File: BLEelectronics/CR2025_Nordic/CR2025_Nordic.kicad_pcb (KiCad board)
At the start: 2 copper layers, 24 parts, among them Q1 Si2307CDS, U1 LP5907MFX-3.3, U2 BAT-HLD-001, U3 LTC4412xS6, U4 LTC4054LES5-4.2#TRPBF, U5 MX25R6435FM2IL0

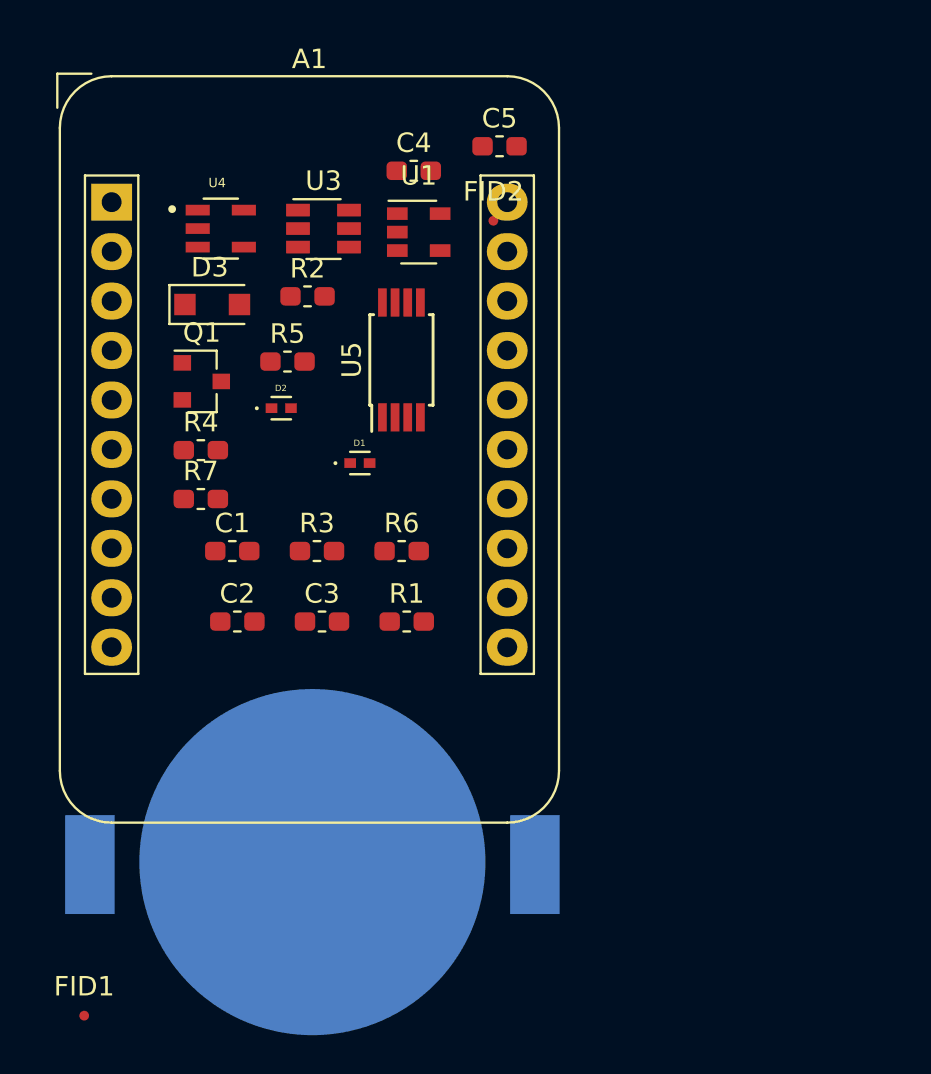
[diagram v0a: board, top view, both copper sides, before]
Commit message: Completed Nordic Dongle adaptor. DRC clean. Ready for review
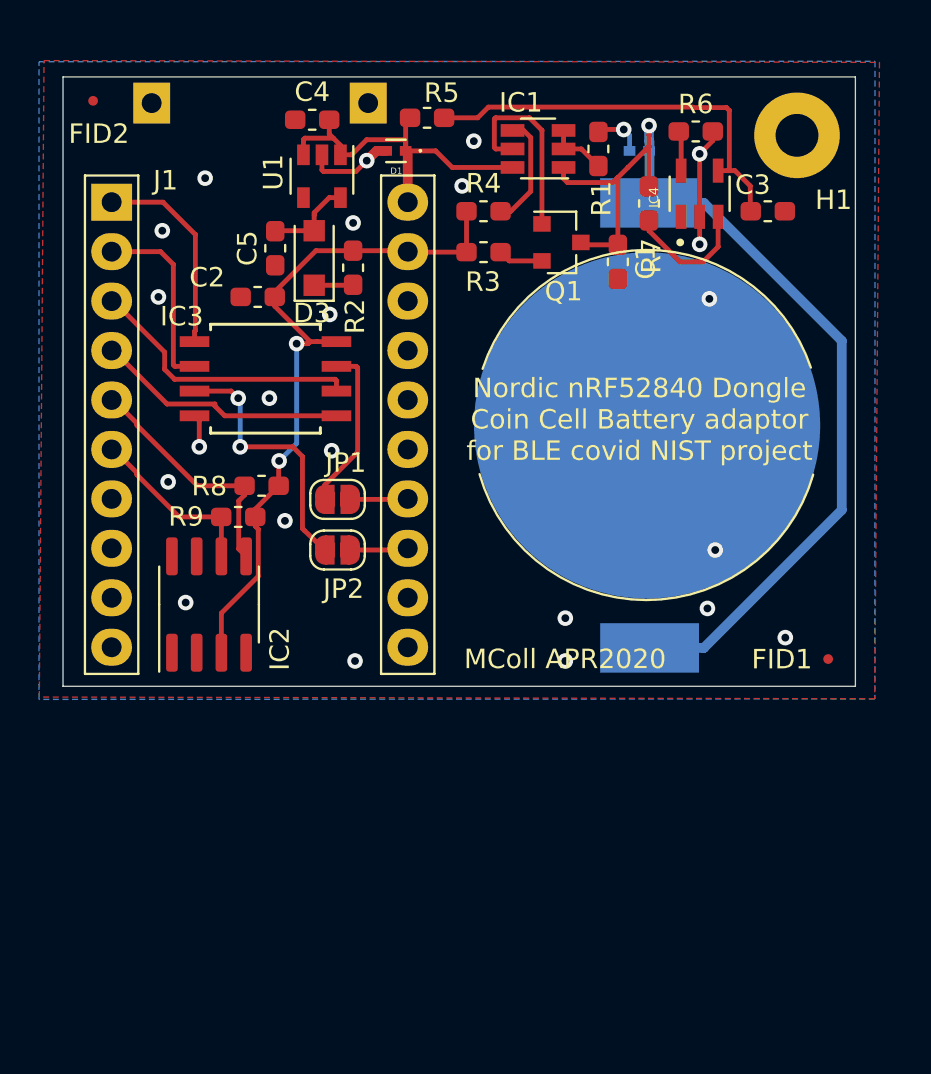
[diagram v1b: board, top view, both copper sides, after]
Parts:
- removed U5: MX25R6435FM2IL0, Package_SO:TSSOP-8_4.4x3mm_P0.65mm
- added H1: MountingHole, MountingHole:MountingHole_2.2mm_M2_Pad, F.Cu at (162.0, 75.7)
- added IC2: PCF8523T, Package_SO:SOIC-8_3.9x4.9mm_P1.27mm, F.Cu at (131.8, 99.8)
- added IC3: MX25R6435FM2IL0, 0my_footprints:MX25R6435FM2IL0, F.Cu at (134.7, 88.2)
- added JP1: Jumper_2_Open, Jumper:SolderJumper-2_P1.3mm_Open_RoundedPad1.0x1.5mm, F.Cu at (138.4, 94.4)
- added JP2: Jumper_2_Open, Jumper:SolderJumper-2_P1.3mm_Open_RoundedPad1.0x1.5mm, F.Cu at (138.4, 97.0)
- added R8: 4.7K, Resistor_SMD:R_0603_1608Metric_Pad1.05x0.95mm_HandSolder, F.Cu at (134.5, 93.7)
- added R9: 4.7K, Resistor_SMD:R_0603_1608Metric_Pad1.05x0.95mm_HandSolder, F.Cu at (133.3, 95.3)
- D2: moved to B.Cu
- J1: renamed from A1; footprint Module:Adafruit_HUZZAH_ESP8266_breakout -> 0my_footprints:Nordic_nRF52840_FeatherHeader
- moved FID1 42.4 mm to (163.6, 102.6)
- moved C3 31.1 mm to (160.5, 79.6)
- moved U2 28.3 mm to (154.3, 90.6), turned to 90 degrees
- moved R7 27.6 mm to (154.4, 79.2), turned to 270 degrees
- moved R6 26.3 mm to (156.8, 75.5)
- moved R1 26.2 mm to (151.8, 76.4), turned to 90 degrees
- moved C1 24.8 mm to (152.8, 82.2), turned to 270 degrees
- moved IC4 24.7 mm to (157.0, 78.7), turned to 90 degrees
- moved D2 22.6 mm to (153.9, 76.5)
- moved FID2 21.5 mm to (125.8, 73.9)
- moved Q1 19.8 mm to (149.9, 81.2)
- moved R4 19.0 mm to (145.9, 79.6)
- moved R3 17.6 mm to (145.9, 81.7)
- moved C2 16.7 mm to (134.3, 84.0), turned to 180 degrees
- moved D1 16.1 mm to (141.4, 76.5), turned to 180 degrees
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- renumbered U3 to IC1, U4 to IC4
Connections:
- C4 pad 2: Net-(C4-Pad2) -> /5Vusb
- D3 pad 1: Net-(C4-Pad2) -> Net-(D3-Pad1)
- D3 pad 2: /5Vusb -> Net-(C5-Pad2)
- J1 pad 1: Net-(A1-Pad1) -> /CS
- J1 pad 2: Net-(A1-Pad2) -> /SO
- J1 pad 3: Net-(A1-Pad3) -> /SCLK
- J1 pad 4: Net-(A1-Pad4) -> /SI
- J1 pad 5: Net-(A1-Pad5) -> /SDA
- J1 pad 6: Net-(A1-Pad6) -> /SCL
- R2 pad 2: Net-(C5-Pad2) -> Net-(D3-Pad1)
- U1 pad 1: Net-(C4-Pad2) -> /5Vusb
- U1 pad 2: Net-(U1-Pad2) -> GND
- U1 pad 3: Net-(C4-Pad2) -> /5Vusb
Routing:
- net /3V: track 0.00 -> 53.0 mm, vias 0 -> 1
- net /VDD_3V: track 0.00 -> 35.9 mm, vias 0 -> 2
- net Net-(C3-Pad1): track 0.00 -> 21.3 mm
- net /5Vusb: track 0.00 -> 18.9 mm
- net GND: track 0.00 -> 15.2 mm, vias 0 -> 24
- net /SCLK: track 0.00 -> 14.3 mm
- net /WP: track 0.00 -> 13.9 mm, vias 0 -> 2
- net /SI: track 0.00 -> 13.0 mm
- net /SDA: track 0.00 -> 12.6 mm
- net /CS: track 0.00 -> 10.5 mm
- net Net-(IC1-Pad5): track 0.00 -> 9.97 mm
- net /SO: track 0.00 -> 9.72 mm
- net /SCL: track 0.00 -> 9.15 mm
- net /RESET: track 0.00 -> 8.57 mm
- net Net-(IC4-Pad3): track 0.00 -> 6.60 mm
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- added copper zone on B.Cu, net GND
- added copper zone on F.Cu, net GND
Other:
- board outline added: 40.7 x 31.3 mm
- board text added: "MColl APR2020"
- board text added: "Nordic nRF52840 Dongle Coin Cell Battery adaptor for BLE covid NIST project"

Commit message: Updated schematic: jumper bypass MOSFET, clock out to header, WP moved to fast IO, fixed library refs, ass spare MOSFET from LTC4412 datasheet.
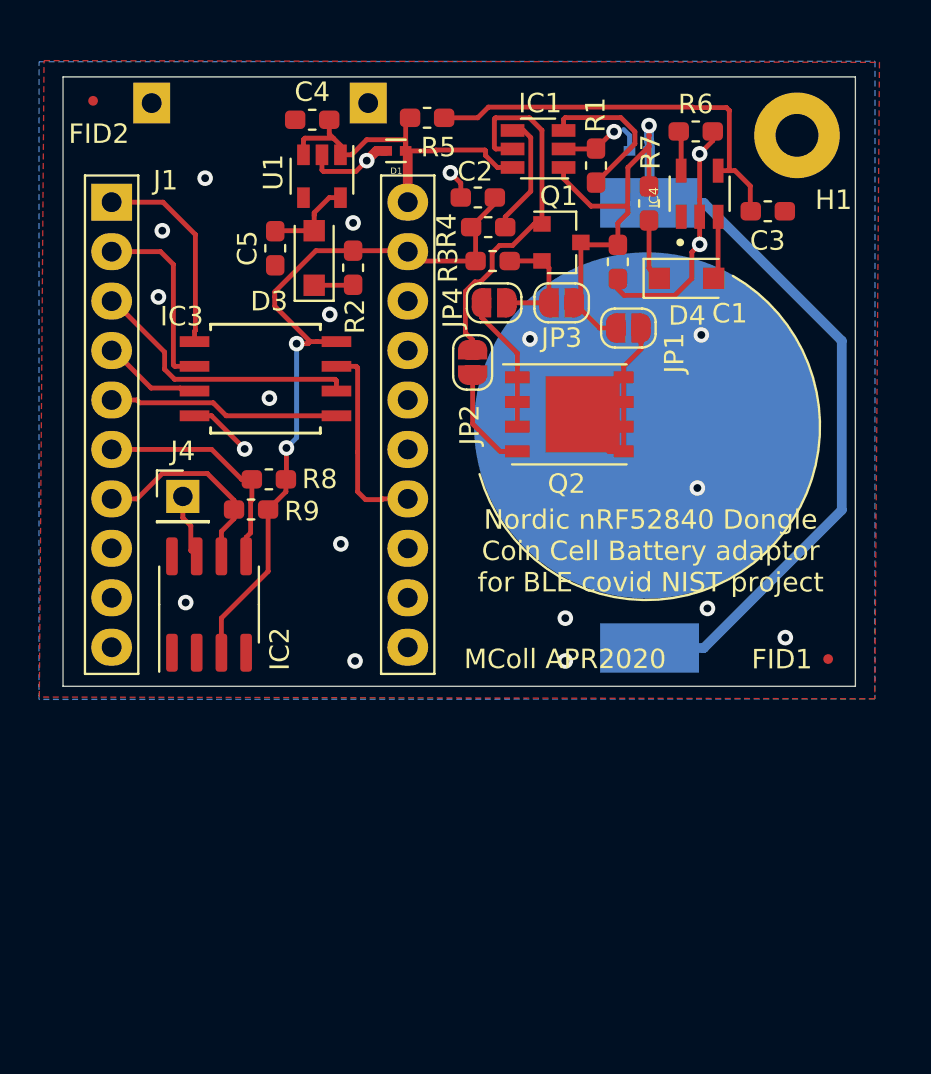
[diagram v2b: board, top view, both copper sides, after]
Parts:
- added D4: D_Schottky, Diode_SMD:D_SOD-123F, F.Cu at (156.3, 83.0)
- added J4: Conn_01x01_Female, Connector_PinHeader_2.54mm:PinHeader_1x01_P2.54mm_Vertical, F.Cu at (130.5, 94.2)
- added JP3: Jumper_2_Open, Jumper:SolderJumper-2_P1.3mm_Open_RoundedPad1.0x1.5mm, F.Cu at (149.9, 84.3)
- added JP4: Jumper_2_Open, Jumper:SolderJumper-2_P1.3mm_Open_RoundedPad1.0x1.5mm, F.Cu at (146.4, 84.3)
- added Q2: Si7463DP, Package_SO:PowerPAK_SO-8_Single, F.Cu at (150.3, 90.0)
- moved JP1 17.3 mm to (153.3, 85.6)
- moved C2 12.4 mm to (145.6, 78.9)
- moved JP2 11.9 mm to (145.3, 87.4), turned to 270 degrees
- moved R1 0.86 mm to (151.7, 77.3)
- moved R4 0.85 mm to (146.1, 80.4)
- moved R9 0.76 mm to (134.0, 94.9)
- moved R3 0.65 mm to (146.4, 82.2)
- moved R8 0.50 mm to (134.9, 93.4)
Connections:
- H1 pad 1: GND -> (no net)
- IC1 pad 2: Net-(IC1-Pad2) -> GND
- IC1 pad 3: Net-(IC1-Pad2) -> Net-(IC1-Pad3)
- IC4 pad 3: Net-(IC4-Pad3) -> Net-(D4-Pad2)
- J1 pad 14: Net-(J1-Pad14) -> /RESET
- J1 pad 4: /SI -> /WP
- J1 pad 5: /SDA -> /SI
- J1 pad 6: /SCL -> /SDA
- J1 pad 7: Net-(J1-Pad7) -> /SCL
- JP1 pad 1: Net-(J1-Pad14) -> Net-(JP1-Pad1)
- JP1 pad 2: /RESET -> /3V
- JP2 pad 1: Net-(J1-Pad13) -> Net-(IC1-Pad5)
- JP2 pad 2: /WP -> Net-(JP2-Pad2)
- R1 pad 1: Net-(IC1-Pad2) -> Net-(IC1-Pad3)
- R7 pad 2: Net-(IC4-Pad3) -> Net-(D4-Pad1)
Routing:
- net GND: track 15.2 -> 26.3 mm, vias 24 -> 22
- net Net-(JP1-Pad1): track 0.00 -> 9.93 mm
- net Net-(IC1-Pad5): track 9.97 -> 19.0 mm
- net /WP: track 13.9 -> 5.12 mm, vias 2 -> 0
- net Net-(IC1-Pad3): track 0.00 -> 8.02 mm
- net Net-(JP4-Pad1): track 0.00 -> 7.13 mm
- net /3V: track 53.0 -> 59.7 mm
- net Net-(IC4-Pad3): track 6.60 -> 0.00 mm
- net Net-(JP2-Pad2): track 0.00 -> 5.39 mm
- net Net-(JP3-Pad2): track 2.31 -> 6.13 mm
- net Net-(IC2-Pad7): track 0.00 -> 3.37 mm
- net Net-(D4-Pad2): track 0.00 -> 3.25 mm
- net Net-(D4-Pad1): track 0.00 -> 3.19 mm
- net Net-(IC1-Pad2): track 3.10 -> 0.00 mm
- net Net-(J1-Pad13): track 2.99 -> 0.00 mm
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
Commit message: tweaks to nordic dongle adaptor.
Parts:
- removed D1, D2: TPD1E10B06DPYR, 0my_footprints:DIODFN100X60X45-2N
- added U3: ESD401, 0my_footprints:ESD401DPYR, B.Cu at (153.9, 76.5)
- added U4: ESD401, 0my_footprints:ESD401DPYR, F.Cu at (141.5, 76.6)
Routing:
- net GND: track 26.3 -> 26.9 mm
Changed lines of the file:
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@@
     (thickness 1.6)
     (drawings 9)
-    (tracks 268)
+    (tracks 270)
     (zones 0)
     (modules 35)
@@
       (outputformat 1)
       (mirror false)
-      (drillshape 1)
+      (drillshape 0)
       (scaleselection 1)
-      (outputdirectory ""))
+      (outputdirectory "gerbers/v1/"))
   )
   (net 0 "")
@@
     (add_net "Net-(U1-Pad4)")
   )
-  (module 0my_footprints:DIODFN100X60X45-2N (layer B.Cu)
-    (at 153.9 76.5)
-    (fp_text reference D2 (at -0.019 1.0282) (layer B.SilkS)
-      (effects (font (size 0.32 0.32) (thickness 0.015)) (justify mirror))
-    )
-    (fp_text value TPD1E10B06DPYR (at 2.6226 -0.9968) (layer B.Fab)
-      (effects (font (size 0.32 0.32) (thickness 0.015)) (justify mirror))
-    )
-    (fp_circle (center -1.256 -0.006) (end -1.206 -0.006) (layer B.Fab) (width 0.1))
-    (fp_line (start -0.5 -0.575) (end 0.5 -0.575) (layer B.SilkS) (width 0.127))
-    (fp_line (start -0.5 0.575) (end 0.5 0.575) (layer B.SilkS) (width 0.127))
-    (fp_circle (center -1.256 -0.006) (end -1.206 -0.006) (layer B.SilkS) (width 0.1))
-    (fp_line (start -1.05 -0.6) (end -1.05 0.6) (layer B.CrtYd) (width 0.05))
-    (fp_line (start 1.05 -0.6) (end -1.05 -0.6) (layer B.CrtYd) (width 0.05))
-    (fp_line (start 1.05 0.6) (end 1.05 -0.6) (layer B.CrtYd) (width 0.05))
-    (fp_line (start -1.05 0.6) (end 1.05 0.6) (layer B.CrtYd) (width 0.05))
-    (fp_line (start -0.55 -0.35) (end -0.55 0.35) (layer B.Fab) (width 0.127))
-    (fp_line (start 0.55 -0.35) (end -0.55 -0.35) (layer B.Fab) (width 0.127))
-    (fp_line (start 0.55 0.35) (end 0.55 -0.35) (layer B.Fab) (width 0.127))
-    (fp_line (start -0.55 0.35) (end 0.55 0.35) (layer B.Fab) (width 0.127))
-    (pad 2 smd rect (at 0.5 0) (size 0.6 0.5) (layers B.Cu B.Paste B.Mask)
+  (module 0my_footprints:ESD401DPYR (layer F.Cu)
+    (at 141.4907 76.5556 180)
+    (fp_text reference U4 (at 0 0) (layer F.SilkS)
+      (effects (font (size 1 1) (thickness 0.15)))
+    )
+    (fp_text value ESD401 (at 0 0) (layer F.SilkS) hide
+      (effects (font (size 1 1) (thickness 0.15)))
+    )
+    (fp_line (start -0.550001 0.350002) (end -0.550001 -0.350002) (layer F.Fab) (width 0.1524))
+    (fp_line (start -0.550001 0.350002) (end 0.550001 0.350002) (layer F.Fab) (width 0.1524))
+    (fp_line (start 0.550001 0.350002) (end 0.550001 -0.350002) (layer F.Fab) (width 0.1524))
+    (fp_line (start -0.550001 -0.350002) (end 0.550001 -0.350002) (layer F.Fab) (width 0.1524))
+    (pad 1 smd rect (at -0.499999 0 180) (size 0.599999 0.499999) (layers F.Cu F.Paste F.Mask)
+      (net 4 /5Vusb))
+    (pad 2 smd rect (at 0.499999 0 180) (size 0.599999 0.499999) (layers F.Cu F.Paste F.Mask)
+      (net 1 GND))
+  )
+  (module 0my_footprints:ESD401DPYR (layer B.Cu)
+    (at 153.903299 76.5175)
+    (fp_text reference U3 (at 0 0) (layer B.SilkS)
+      (effects (font (size 1 1) (thickness 0.15)) (justify mirror))
+    )
+    (fp_text value ESD401 (at 0 0) (layer B.SilkS) hide
+      (effects (font (size 1 1) (thickness 0.15)) (justify mirror))
+    )
+    (fp_line (start -0.550001 -0.350002) (end -0.550001 0.350002) (layer B.Fab) (width 0.1524))
+    (fp_line (start -0.550001 -0.350002) (end 0.550001 -0.350002) (layer B.Fab) (width 0.1524))
+    (fp_line (start 0.550001 -0.350002) (end 0.550001 0.350002) (layer B.Fab) (width 0.1524))
+    (fp_line (start -0.550001 0.350002) (end 0.550001 0.350002) (layer B.Fab) (width 0.1524))
+    (pad 1 smd rect (at -0.499999 0) (size 0.599999 0.499999) (layers B.Cu B.Paste B.Mask)
+      (net 1 GND))
+    (pad 2 smd rect (at 0.499999 0) (size 0.599999 0.499999) (layers B.Cu B.Paste B.Mask)
       (net 2 /3V))
-    (pad 1 smd rect (at -0.5 0) (size 0.6 0.5) (layers B.Cu B.Paste B.Mask)
-      (net 1 GND))
-  )
-  (module 0my_footprints:DIODFN100X60X45-2N (layer F.Cu)
-    (at 141.4 76.5 180)
-    (fp_text reference D1 (at -0.019 -1.0282) (layer F.SilkS)
-      (effects (font (size 0.32 0.32) (thickness 0.015)))
-    )
-    (fp_text value TPD1E10B06DPYR (at 2.6226 0.9968) (layer F.Fab)
-      (effects (font (size 0.32 0.32) (thickness 0.015)))
-    )
-    (fp_circle (center -1.256 0.006) (end -1.206 0.006) (layer F.Fab) (width 0.1))
-    (fp_line (start -0.5 0.575) (end 0.5 0.575) (layer F.SilkS) (width 0.127))
-    (fp_line (start -0.5 -0.575) (end 0.5 -0.575) (layer F.SilkS) (width 0.127))
-    (fp_circle (center -1.256 0.006) (end -1.206 0.006) (layer F.SilkS) (width 0.1))
-    (fp_line (start -1.05 0.6) (end -1.05 -0.6) (layer F.CrtYd) (width 0.05))
-    (fp_line (start 1.05 0.6) (end -1.05 0.6) (layer F.CrtYd) (width 0.05))
-    (fp_line (start 1.05 -0.6) (end 1.05 0.6) (layer F.CrtYd) (width 0.05))
-    (fp_line (start -1.05 -0.6) (end 1.05 -0.6) (layer F.CrtYd) (width 0.05))
-    (fp_line (start -0.55 0.35) (end -0.55 -0.35) (layer F.Fab) (width 0.127))
-    (fp_line (start 0.55 0.35) (end -0.55 0.35) (layer F.Fab) (width 0.127))
-    (fp_line (start 0.55 -0.35) (end 0.55 0.35) (layer F.Fab) (width 0.127))
-    (fp_line (start -0.55 -0.35) (end 0.55 -0.35) (layer F.Fab) (width 0.127))
-    (pad 2 smd rect (at 0.5 0 180) (size 0.6 0.5) (layers F.Cu F.Paste F.Mask)
-      (net 1 GND))
-    (pad 1 smd rect (at -0.5 0 180) (size 0.6 0.5) (layers F.Cu F.Paste F.Mask)
-      (net 4 /5Vusb))
   )
   (module Capacitor_SMD:C_0603_1608Metric_Pad1.05x0.95mm_HandSolder (layer F.Cu)
@@
       (effects (font (size 1 1) (thickness 0.15)))
     )
+    (fp_text user %R (at 0.3 0) (layer F.Fab)
+      (effects (font (size 1 1) (thickness 0.15)))
+    )
+    (fp_circle (center 0 0) (end 2.2 0) (layer Cmts.User) (width 0.15))
     (fp_circle (center 0 0) (end 2.45 0) (layer F.CrtYd) (width 0.05))
-    (fp_circle (center 0 0) (end 2.2 0) (layer Cmts.User) (width 0.15))
-    (fp_text user %R (at 0.3 0) (layer F.Fab)
-      (effects (font (size 1 1) (thickness 0.15)))
-    )
     (pad 1 thru_hole circle (at 0 0) (size 4.4 4.4) (drill 2.2) (layers *.Cu *.Mask))
   )
@@
       (effects (font (size 1 1) (thickness 0.15)))
     )
-    (fp_circle (center 0 0) (end 0.75 0) (layer F.CrtYd) (width 0.05))
+    (fp_circle (center 0 0) (end 0.5 0) (layer F.Fab) (width 0.1))
     (fp_text user %R (at 0 0) (layer F.Fab)
       (effects (font (size 0.2 0.2) (thickness 0.04)))
     )
-    (fp_circle (center 0 0) (end 0.5 0) (layer F.Fab) (width 0.1))
+    (fp_circle (center 0 0) (end 0.75 0) (layer F.CrtYd) (width 0.05))
     (pad "" smd circle (at 0 0) (size 0.5 0.5) (layers F.Cu F.Mask)
       (solder_mask_margin 0.25) (clearance 0.25))
@@
       (effects (font (size 1 1) (thickness 0.15)))
     )
-    (fp_circle (center 0 0) (end 0.75 0) (layer F.CrtYd) (width 0.05))
+    (fp_circle (center 0 0) (end 0.5 0) (layer F.Fab) (width 0.1))
     (fp_text user %R (at 0 0) (layer F.Fab)
       (effects (font (size 0.2 0.2) (thickness 0.04)))
     )
-    (fp_circle (center 0 0) (end 0.5 0) (layer F.Fab) (width 0.1))
+    (fp_circle (center 0 0) (end 0.75 0) (layer F.CrtYd) (width 0.05))
     (pad "" smd circle (at 0 0) (size 0.5 0.5) (layers F.Cu F.Mask)
       (solder_mask_margin 0.25) (clearance 0.25))
@@
   (segment (start 144.7305 78.1571) (end 144.1958 77.6224) (width 0.25) (layer F.Cu) (net 1))
   (segment (start 144.7305 78.8924) (end 144.7305 78.1571) (width 0.25) (layer F.Cu) (net 1))
+  (segment (start 152.7174 75.4) (end 152.6032 75.5142) (width 0.25) (layer B.Cu) (net 1))
+  (segment (start 153.1 75.4) (end 152.7174 75.4) (width 0.25) (layer B.Cu) (net 1))
   (segment (start 157.217 102.03) (end 164.3 94.947) (width 0.5) (layer B.Cu) (net 2))
   (segment (start 154.427 102.03) (end 157.217 102.03) (width 0.5) (layer B.Cu) (net 2))
